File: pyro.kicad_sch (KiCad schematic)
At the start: 6 parts, among them J6 Pyro, Q2 BSC098N10NS5

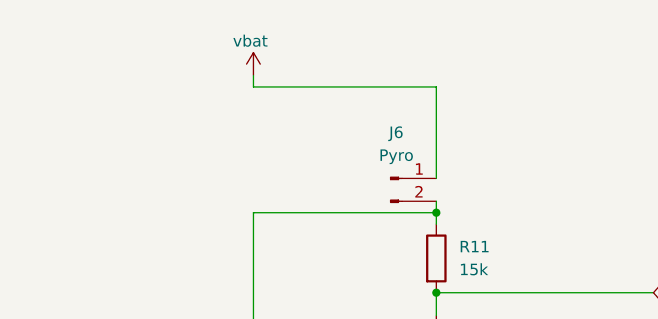
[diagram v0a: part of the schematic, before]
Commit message: began fixing schematic added barometer
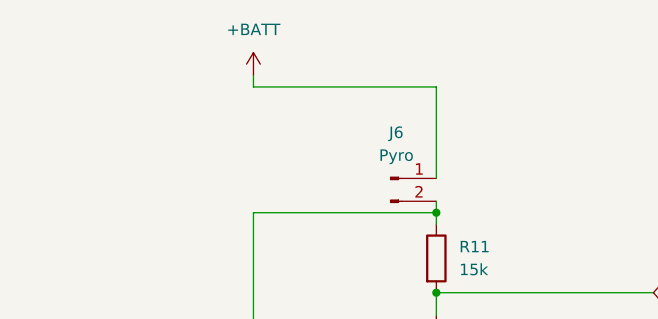
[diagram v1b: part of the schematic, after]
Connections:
- net vbat renamed +BATT
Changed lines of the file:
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@@
+	)
+	(symbol
+		(lib_id "power:+BATT")
+		(at 134.62 44.45 0)
+		(unit 1)
+		(exclude_from_sim no)
+		(in_bom yes)
+		(on_board yes)
+		(dnp no)
+		(fields_autoplaced yes)
+		(property "Reference" "#PWR07"
+			(at 134.62 48.26 0)
+			(effects
+				(font
+					(size 1.27 1.27)
+				)
+				(hide yes)
+			)
+		)
+		(property "Value" "+BATT"
+			(at 134.62 39.37 0)
+			(effects
+				(font
+					(size 1.27 1.27)
+				)
+			)
+		)
+		(property "Footprint" ""
+			(at 134.62 44.45 0)
+			(effects
+				(font
+					(size 1.27 1.27)
+				)
+				(hide yes)
+			)
+		)
+		(property "Datasheet" ""
+			(at 134.62 44.45 0)
+			(effects
+				(font
+					(size 1.27 1.27)
+				)
+				(hide yes)
+			)
+		)
+		(property "Description" "Power symbol creates a global label with name \"+BATT\""
+			(at 134.62 44.45 0)
+			(effects
+				(font
+					(size 1.27 1.27)
+				)
+				(hide yes)
+			)
+		)
+		(pin "1"
+		)
+		(instances
+			(project ""
+				(path "/6cb3dda3-5fe8-4715-b831-354360aa3199/00a4b53a-09dd-45fe-9668-74427c57713f"
+					(reference "#PWR07")
+					(unit 1)
+				)
+			)
+		)
 	)
 	(symbol
@@
 					(unit 1)
 				)
-			)
-		)
-	)
-	(symbol
-		(lib_id "power:+7.5V")
-		(at 134.62 44.45 0)
-		(unit 1)
-		(exclude_from_sim no)
-		(in_bom yes)
-		(on_board yes)
-		(dnp no)
-		(property "Reference" "#PWR0101"
-			(at 134.62 48.26 0)
-			(effects
-				(font
-					(size 1.27 1.27)
-				)
-				(hide yes)
-			)
-		)
-		(property "Value" "vbat"
-			(at 132.334 40.64 0)
-			(effects
-				(font
-					(size 1.27 1.27)
-				)
-				(justify left)
-			)
-		)
-		(property "Footprint" ""
-			(at 134.62 44.45 0)
-			(effects
-				(font
-					(size 1.27 1.27)
-				)
-				(hide yes)
-			)
-		)
-		(property "Datasheet" ""
-			(at 134.62 44.45 0)
-			(effects
-				(font
-					(size 1.27 1.27)
-				)
-				(hide yes)
-			)
-		)
-		(property "Description" "Power symbol creates a global label with name \"+7.5V\""
-			(at 134.62 44.45 0)
-			(effects
-				(font
-					(size 1.27 1.27)
-				)
-				(hide yes)
-			)
-		)
-		(pin "1"
-		)
-		(instances
-			(project "flightcomputer2"
-				(path "/6cb3dda3-5fe8-4715-b831-354360aa3199/00a4b53a-09dd-45fe-9668-74427c57713f"
-					(reference "#PWR0101")
-					(unit 1)
-				)
